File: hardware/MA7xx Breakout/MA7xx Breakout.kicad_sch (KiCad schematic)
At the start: 11 parts, among them IC1 MA702GQ-P, U2 MIC5504-3.3YM5

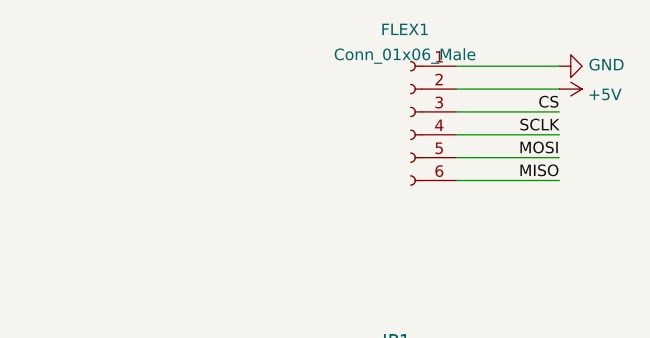
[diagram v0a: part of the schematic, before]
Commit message: update to R2.1
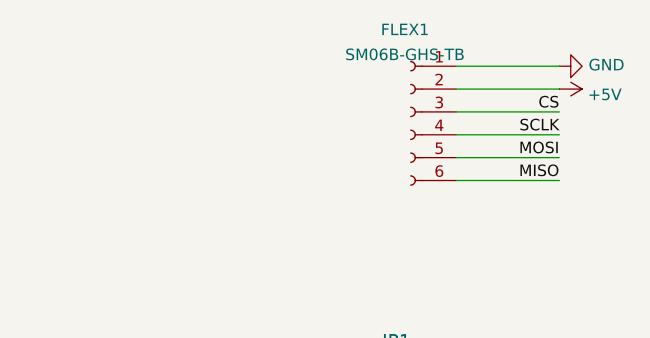
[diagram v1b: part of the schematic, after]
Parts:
- FLEX1: value Conn_01x06_Male -> SM06B-GHS-TB
- H1, H2, JP1, JP2, JP3: now left out of the parts list
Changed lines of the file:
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@@
   )
   (symbol (lib_id "MA702-eagle-import:PINHD-1X06_2.54-S") (at 242.57 69.215 0) (unit 1)
-    (in_bom yes) (on_board yes) (dnp no)
+    (in_bom no) (on_board yes) (dnp no)
     (property "Reference" "JP1" (at 236.22 58.42 0)
       (effects (font (size 1.778 1.5113)) (justify left bottom))
@@
   )
   (symbol (lib_id "Mechanical:MountingHole") (at 239.395 170.815 0) (unit 1)
-    (in_bom yes) (on_board yes) (dnp no) (fields_autoplaced)
+    (in_bom no) (on_board yes) (dnp no) (fields_autoplaced)
     (property "Reference" "H1" (at 242.57 170.18 0)
       (effects (font (size 1.27 1.27)) (justify left))
@@
   )
   (symbol (lib_id "MA702-eagle-import:PINHD-1X02_2.54-S") (at 242.57 143.51 0) (unit 1)
-    (in_bom yes) (on_board yes) (dnp no)
+    (in_bom no) (on_board yes) (dnp no)
     (property "Reference" "JP3" (at 236.22 137.795 0)
       (effects (font (size 1.778 1.5113)) (justify left bottom))
@@
       (effects (font (size 1.27 1.27)))
     )
-    (property "Value" "Conn_01x06_Male" (at 238.76 25.4024 0)
+    (property "Value" "SM06B-GHS-TB" (at 238.76 25.4024 0)
       (effects (font (size 1.27 1.27)))
     )
@@
   )
   (symbol (lib_id "Mechanical:MountingHole") (at 239.395 182.245 0) (unit 1)
-    (in_bom yes) (on_board yes) (dnp no) (fields_autoplaced)
+    (in_bom no) (on_board yes) (dnp no) (fields_autoplaced)
     (property "Reference" "H2" (at 242.57 181.61 0)
       (effects (font (size 1.27 1.27)) (justify left))
@@
   )
   (symbol (lib_id "MA702-eagle-import:PINHD-1X06_2.54-S") (at 242.57 109.855 0) (unit 1)
-    (in_bom yes) (on_board yes) (dnp no)
+    (in_bom no) (on_board yes) (dnp no)
     (property "Reference" "JP2" (at 236.22 99.06 0)
       (effects (font (size 1.778 1.5113)) (justify left bottom))
